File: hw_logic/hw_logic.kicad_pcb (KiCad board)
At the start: 2 copper layers, 62.2 x 38.1 mm, 8 parts, among them P1 CONN_01X10, SW13 SW_PUSH, U1 LEO_PRO_MICRO, U2 IS25LQ, U3 USB_HOST_SHIELD_MINI

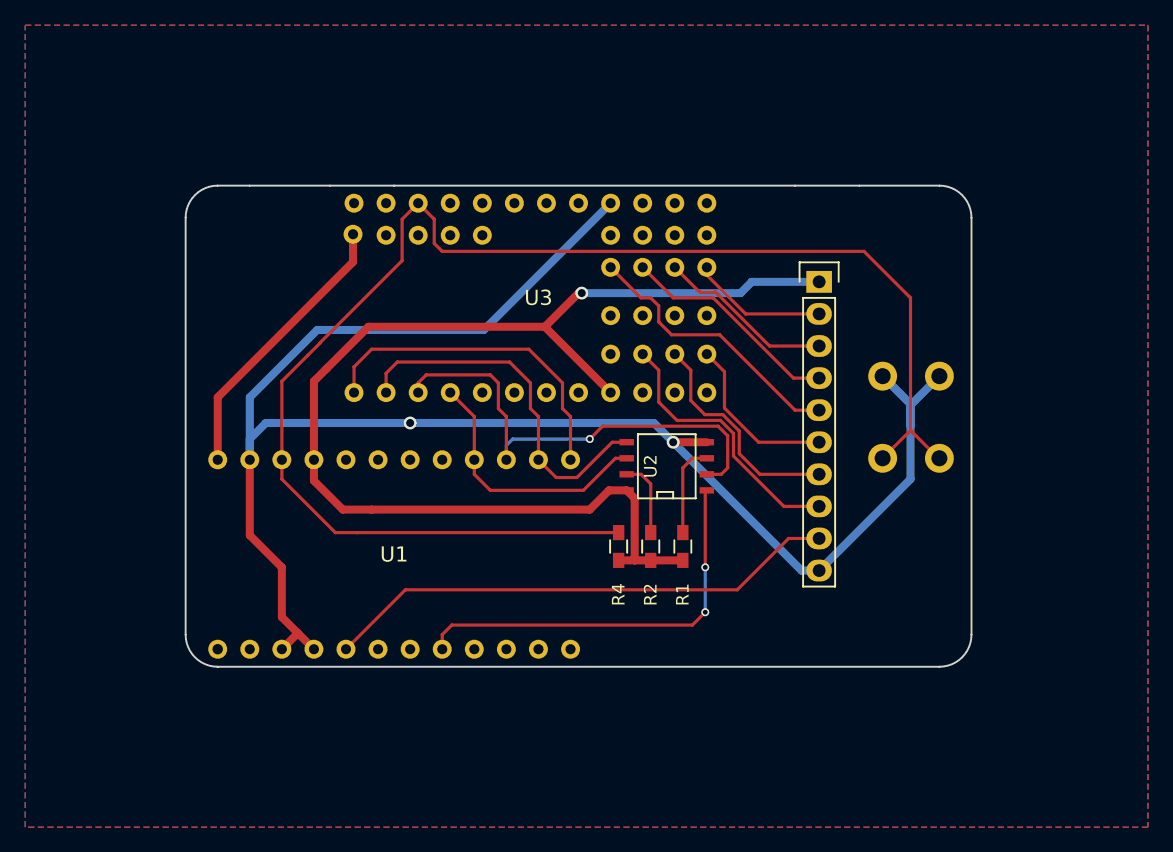
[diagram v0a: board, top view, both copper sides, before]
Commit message: misc, rst button 3d model
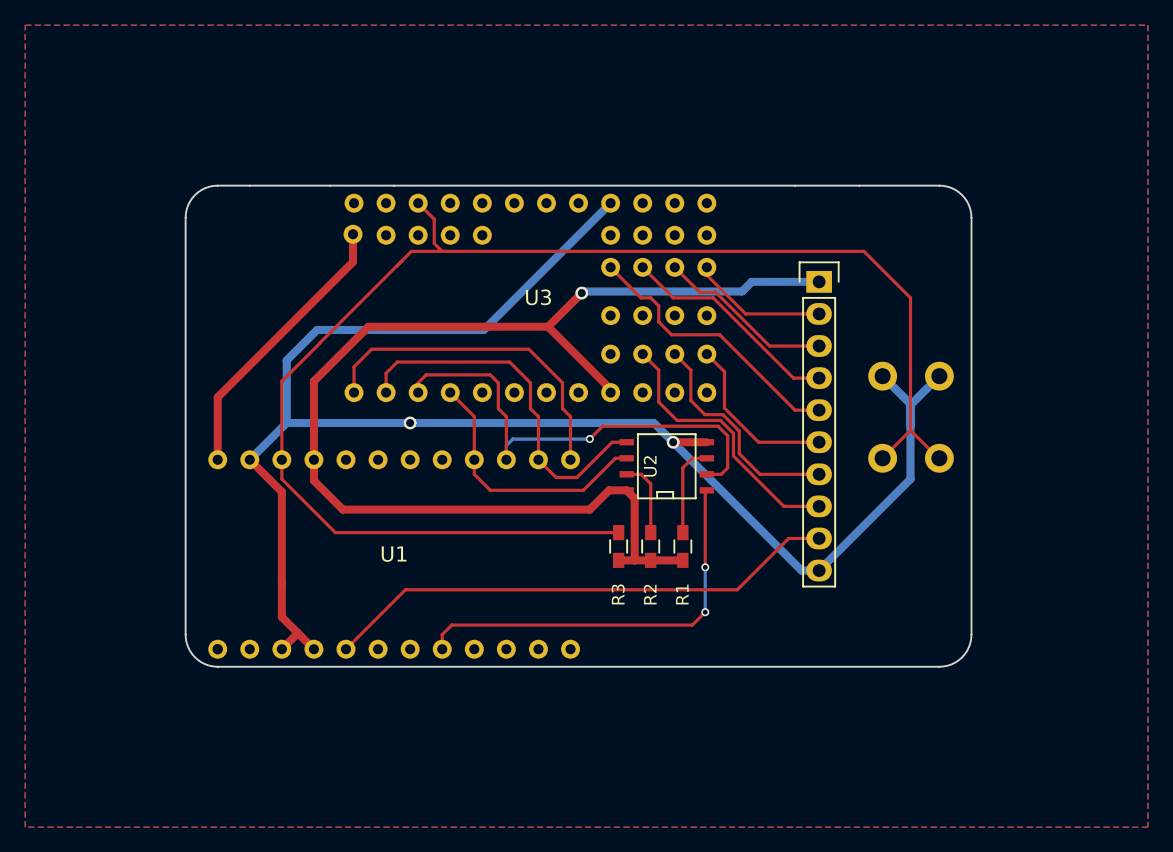
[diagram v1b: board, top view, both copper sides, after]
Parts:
- renumbered R4 to R3
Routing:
- net GND: track 137.8 -> 132.7 mm
- net /RST: track 114.9 -> 114.2 mm

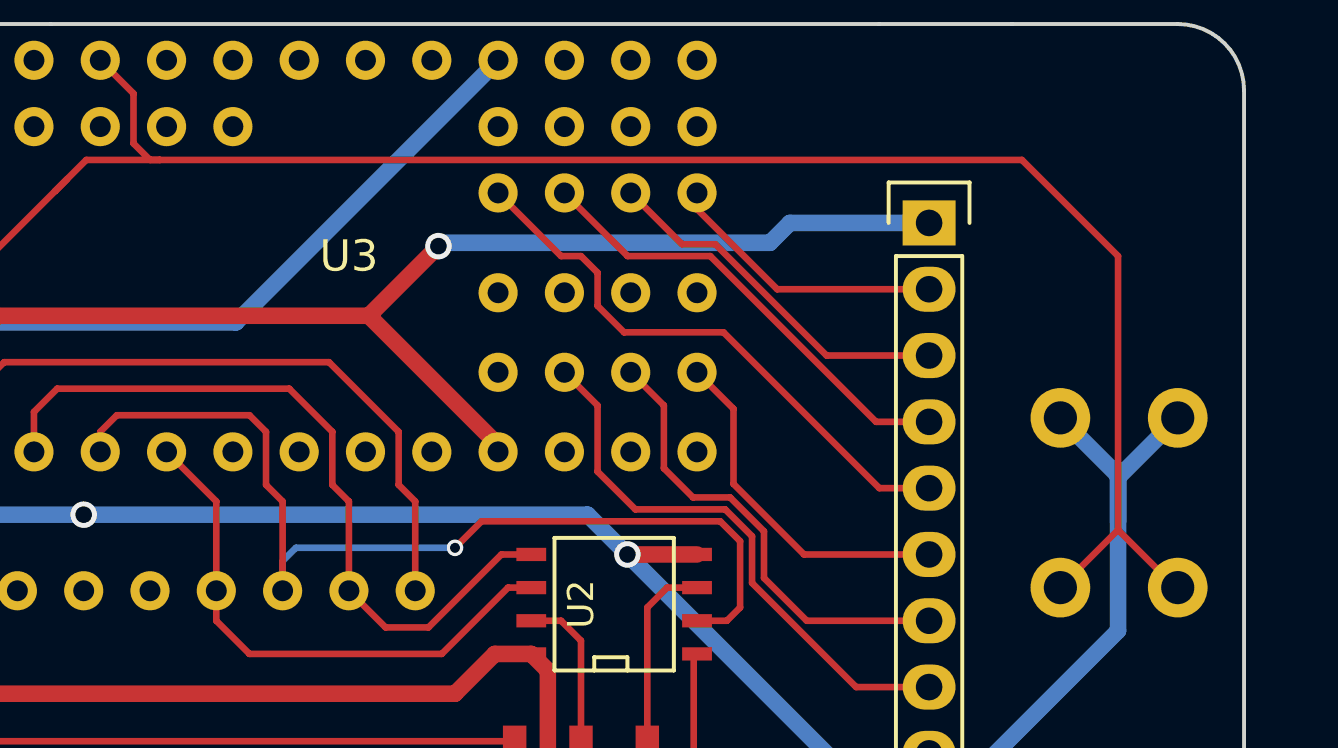
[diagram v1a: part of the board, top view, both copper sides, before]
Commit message: clean up traces, ground fills
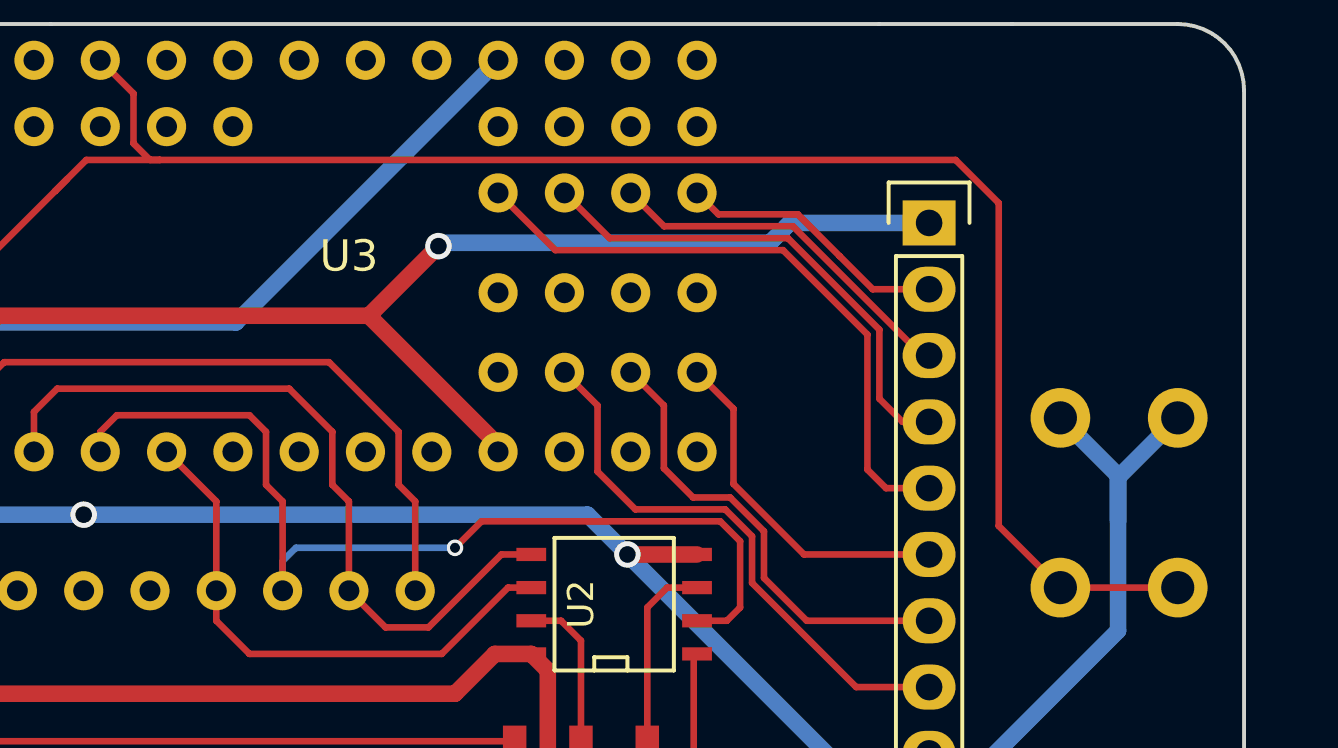
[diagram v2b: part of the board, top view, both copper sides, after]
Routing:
- net /GO3: track 21.9 -> 24.2 mm
- net /RST: track 114.2 -> 112.3 mm
- net /GO2: track 17.6 -> 19.2 mm
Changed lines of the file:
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@@
     (links 36)
     (no_connects 0)
-    (area 12.7 12.7 101.600001 76.200001)
+    (area 25.324999 25.324999 87.705001 63.575001)
     (thickness 1.6)
     (drawings 14)
-    (tracks 174)
+    (tracks 177)
     (zones 0)
     (modules 8)
@@
   (segment (start 65.532 46.99) (end 66.675 46.99) (width 0.254) (layer F.Cu) (net 11) (status 20))
   (segment (start 64.77 47.752) (end 65.532 46.99) (width 0.254) (layer F.Cu) (net 11))
+  (segment (start 80.5942 46.99) (end 85.09 46.99) (width 0.254) (layer F.Cu) (net 12) (status C00000))
+  (segment (start 80.5942 46.99) (end 78.232 44.6278) (width 0.254) (layer F.Cu) (net 12) (status 400000))
+  (segment (start 78.232 32.258) (end 76.581 30.607) (width 0.254) (layer F.Cu) (net 12))
+  (segment (start 78.232 44.6278) (end 78.232 32.258) (width 0.254) (layer F.Cu) (net 12))
   (segment (start 42.086416 31.799416) (end 43.278832 30.607) (width 0.254) (layer F.Cu) (net 12))
   (segment (start 43.278832 30.607) (end 46.101 30.607) (width 0.254) (layer F.Cu) (net 12))
@@
   (segment (start 45.0885 29.9755) (end 45.72 30.607) (width 0.254) (layer F.Cu) (net 12))
   (segment (start 45.72 30.607) (end 46.101 30.607) (width 0.254) (layer F.Cu) (net 12))
-  (segment (start 79.121 30.607) (end 82.804 34.29) (width 0.254) (layer F.Cu) (net 12))
-  (segment (start 82.804 34.29) (end 82.804 44.7802) (width 0.254) (layer F.Cu) (net 12))
-  (segment (start 46.101 30.607) (end 79.121 30.607) (width 0.254) (layer F.Cu) (net 12))
+  (segment (start 46.101 30.607) (end 76.581 30.607) (width 0.254) (layer F.Cu) (net 12))
   (segment (start 85.09 46.99) (end 85.0138 46.99) (width 0.254) (layer F.Cu) (net 12) (status 30))
-  (segment (start 85.0138 46.99) (end 82.804 44.7802) (width 0.254) (layer F.Cu) (net 12) (status 10))
-  (segment (start 82.804 44.7802) (end 80.5942 46.99) (width 0.254) (layer F.Cu) (net 12) (status 20))
+  (segment (start 72.136 34.29) (end 70.535798 32.689798) (width 0.254) (layer F.Cu) (net 13))
+  (segment (start 67.494798 32.689798) (end 66.675 31.87) (width 0.254) (layer F.Cu) (net 13) (status 800000))
+  (segment (start 70.535798 32.689798) (end 67.494798 32.689798) (width 0.254) (layer F.Cu) (net 13))
+  (segment (start 75.565 35.56) (end 73.406 35.56) (width 0.254) (layer F.Cu) (net 13) (status 400000))
+  (segment (start 73.406 35.56) (end 72.136 34.29) (width 0.254) (layer F.Cu) (net 13))
   (segment (start 66.675 31.87) (end 66.675 32.488836) (width 0.254) (layer F.Cu) (net 13) (status 30))
-  (segment (start 66.675 32.488836) (end 69.746164 35.56) (width 0.254) (layer F.Cu) (net 13) (status 10))
-  (segment (start 69.746164 35.56) (end 75.565 35.56) (width 0.254) (layer F.Cu) (net 13) (status 20))
-  (segment (start 64.135 31.87) (end 66.097798 33.832798) (width 0.254) (layer F.Cu) (net 14) (status 10))
-  (segment (start 71.639582 38.1) (end 75.565 38.1) (width 0.254) (layer F.Cu) (net 14) (status 20))
-  (segment (start 67.37238 33.832798) (end 71.639582 38.1) (width 0.254) (layer F.Cu) (net 14))
-  (segment (start 66.097798 33.832798) (end 67.37238 33.832798) (width 0.254) (layer F.Cu) (net 14))
-  (segment (start 61.595 31.87) (end 64.015 34.29) (width 0.254) (layer F.Cu) (net 15) (status 10))
-  (segment (start 73.533 40.64) (end 75.565 40.64) (width 0.254) (layer F.Cu) (net 15) (status 20))
-  (segment (start 67.183 34.29) (end 73.533 40.64) (width 0.254) (layer F.Cu) (net 15))
-  (segment (start 64.015 34.29) (end 67.183 34.29) (width 0.254) (layer F.Cu) (net 15))
+  (segment (start 75.565 38.1) (end 75.299418 38.1) (width 0.254) (layer F.Cu) (net 14) (status C00000))
+  (segment (start 75.299418 38.1) (end 70.346418 33.147) (width 0.254) (layer F.Cu) (net 14) (status 400000))
+  (segment (start 70.346418 33.147) (end 65.412 33.147) (width 0.254) (layer F.Cu) (net 14))
+  (segment (start 65.412 33.147) (end 64.135 31.87) (width 0.254) (layer F.Cu) (net 14) (status 800000))
+  (segment (start 75.565 40.64) (end 74.549 40.64) (width 0.254) (layer F.Cu) (net 15) (status C00000))
+  (segment (start 74.549 40.64) (end 73.66 39.751) (width 0.254) (layer F.Cu) (net 15) (status 400000))
+  (segment (start 73.66 39.751) (end 73.66 37.107164) (width 0.254) (layer F.Cu) (net 15))
+  (segment (start 73.66 37.107164) (end 70.157038 33.604202) (width 0.254) (layer F.Cu) (net 15))
+  (segment (start 70.157038 33.604202) (end 63.329202 33.604202) (width 0.254) (layer F.Cu) (net 15))
+  (segment (start 63.329202 33.604202) (end 61.595 31.87) (width 0.254) (layer F.Cu) (net 15) (status 800000))
+  (segment (start 75.565 43.18) (end 73.914 43.18) (width 0.254) (layer F.Cu) (net 16) (status 400000))
+  (segment (start 61.246404 34.061404) (end 59.055 31.87) (width 0.254) (layer F.Cu) (net 16) (status 800000))
+  (segment (start 69.967658 34.061404) (end 61.246404 34.061404) (width 0.254) (layer F.Cu) (net 16))
+  (segment (start 73.202798 37.296544) (end 69.967658 34.061404) (width 0.254) (layer F.Cu) (net 16))
+  (segment (start 73.202798 42.468798) (end 73.202798 37.296544) (width 0.254) (layer F.Cu) (net 16))
+  (segment (start 73.914 43.18) (end 73.202798 42.468798) (width 0.254) (layer F.Cu) (net 16))
   (segment (start 59.055 31.87) (end 59.055 31.877) (width 0.254) (layer F.Cu) (net 16) (status 30))
-  (segment (start 59.055 31.877) (end 61.468 34.29) (width 0.254) (layer F.Cu) (net 16) (status 10))
-  (segment (start 62.865 36.195) (end 63.881 37.211) (width 0.254) (layer F.Cu) (net 16))
-  (segment (start 62.865 34.925) (end 62.865 36.195) (width 0.254) (layer F.Cu) (net 16))
-  (segment (start 62.23 34.29) (end 62.865 34.925) (width 0.254) (layer F.Cu) (net 16))
-  (segment (start 61.468 34.29) (end 62.23 34.29) (width 0.254) (layer F.Cu) (net 16))
-  (segment (start 73.66 43.18) (end 75.565 43.18) (width 0.254) (layer F.Cu) (net 16) (status 20))
-  (segment (start 67.691 37.211) (end 73.66 43.18) (width 0.254) (layer F.Cu) (net 16))
-  (segment (start 63.881 37.211) (end 67.691 37.211) (width 0.254) (layer F.Cu) (net 16))
   (segment (start 66.675 38.742) (end 68.072 40.139) (width 0.254) (layer F.Cu) (net 17) (status 10))
   (segment (start 70.773746 45.72) (end 75.565 45.72) (width 0.254) (layer F.Cu) (net 17) (status 20))

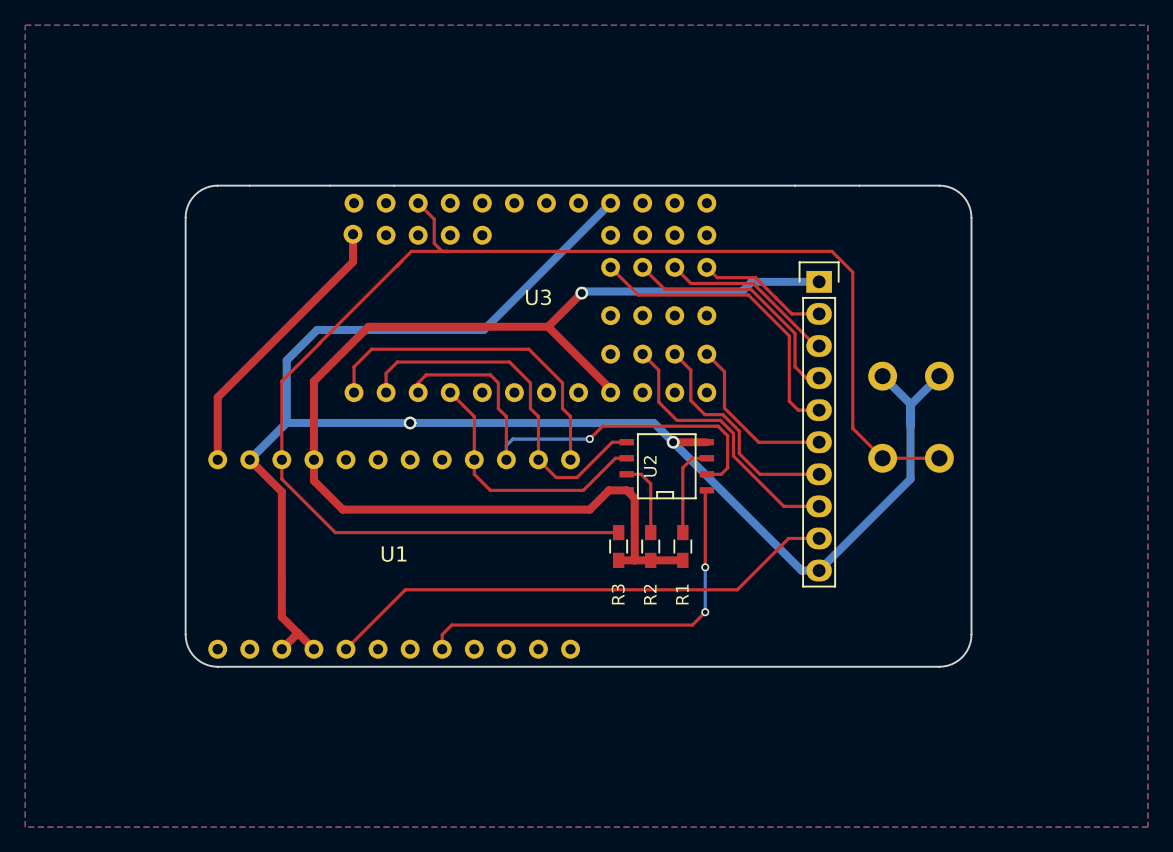
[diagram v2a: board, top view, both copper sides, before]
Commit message: mounting holes
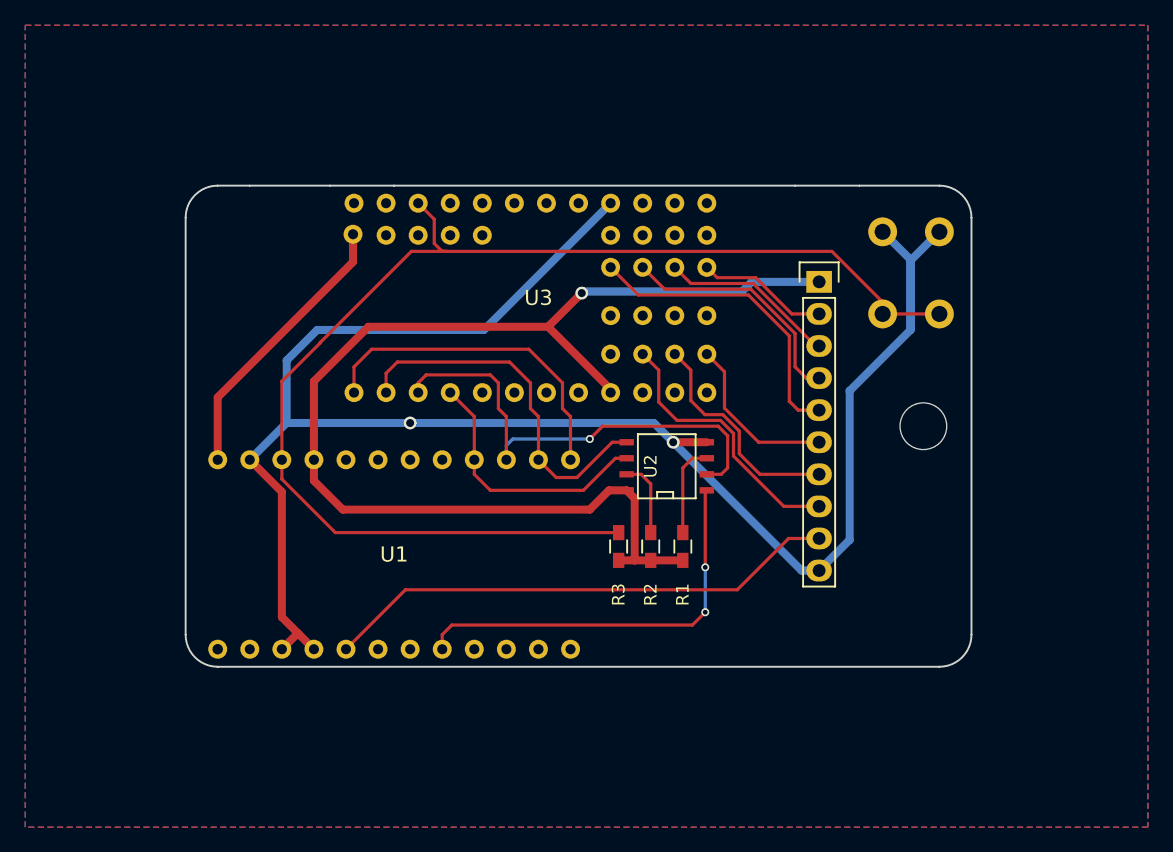
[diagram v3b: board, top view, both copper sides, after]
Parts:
- added REF**: MountingHole_3.7mm, Mounting_Holes:MountingHole_3.7mm, F.Cu at (83.8, 44.5)
- moved SW13 11.4 mm to (85.1, 35.6)
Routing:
- net GND: track 132.7 -> 147.9 mm
- net /RST: track 112.3 -> 100.1 mm

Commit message: correct pin layouts
as per breadboard test
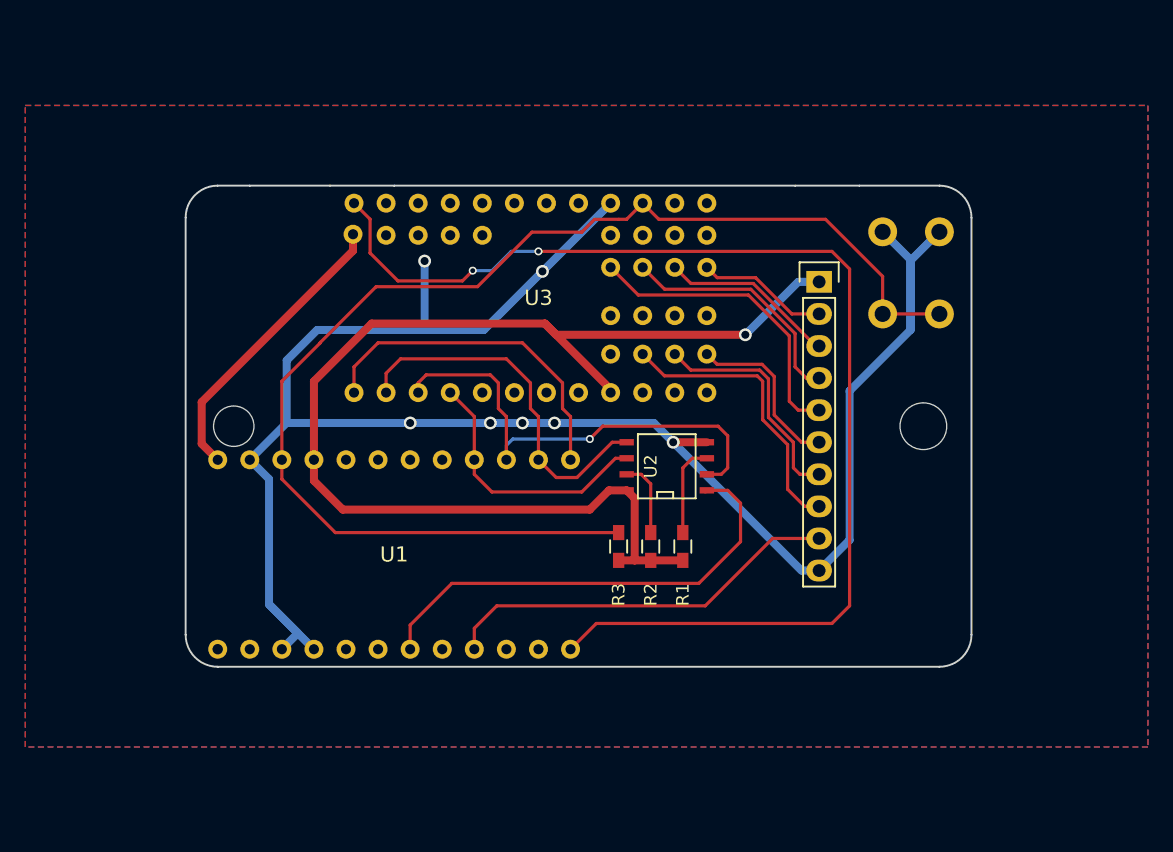
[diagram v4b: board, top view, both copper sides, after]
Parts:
- added REF**: MountingHole_3.2mm_M3, Mounting_Holes:MountingHole_3.2mm_M3, F.Cu at (29.2, 44.5)
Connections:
- U1 pad 12: (no net) -> /USB_INT
- U1 pad 5: /LED_MACRO -> (no net)
- U1 pad 7: (no net) -> /FLASH_SS
- U1 pad 8: /FLASH_SS -> (no net)
- U1 pad 9: (no net) -> /LED_MACRO
- U3 pad 11: (no net) -> GND
- U3 pad 15: (no net) -> /RST
- U3 pad 22: /RST -> (no net)
- U3 pad 24: (no net) -> /USB_INT
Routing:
- net /USB_INT: track 0.00 -> 95.1 mm, vias 0 -> 2
- net /LED_MACRO: track 41.1 -> 31.9 mm
- net GND: track 147.9 -> 156.7 mm, vias 2 -> 7
- net /FLASH_SS: track 32.4 -> 37.1 mm, vias 2 -> 0
- net /GI2: track 21.5 -> 22.8 mm
- net +3V3: track 96.0 -> 97.1 mm
- net +5V: track 22.3 -> 23.4 mm
- net /RST: track 100.1 -> 99.5 mm
- net /GI1: track 17.8 -> 18.3 mm
